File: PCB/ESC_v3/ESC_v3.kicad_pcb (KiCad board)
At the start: 4 copper layers, 42 x 83.5 mm, 133 parts, among them J1 Conn_01x04_Pin, J10 Conn_01x01_Pin, J11 Screw_Terminal_01x01, J2 Screw_Terminal_01x01, J3 Conn_01x01_Pin, J4 Conn_01x01_Pin, J5 Conn_01x01_Pin, J6 Conn_01x01_Pin, J7 Conn_01x01_Pin, J8 Conn_01x01_Pin, J9 Conn_01x01_Pin, Q1 NTMFS2D1N08XT1G, Q2 NTMFS2D1N08XT1G, Q3 NTMFS2D1N08XT1G, Q4 NTMFS2D1N08XT1G, Q5 NTMFS2D1N08XT1G, Q6 NTMFS2D1N08XT1G, U1 SN65HVD232, U2 DRV8323SRTAT, U5 STM32G431CBT6, Y2 16MHz

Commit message: Updates
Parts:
- added C33: 100n, Capacitor_SMD:C_0805_2012Metric, B.Cu at (140.5, 83.0)
- added C34: 100n/6.3V, Capacitor_SMD:C_0805_2012Metric, B.Cu at (138.5, 72.9)
- added C39: 1u/DNP, Capacitor_SMD:C_0805_2012Metric, F.Cu at (149.8, 91.5)
- added C42: 1u/DNP, Capacitor_SMD:C_0805_2012Metric, F.Cu at (149.8, 93.5)
- added C43: 100n, Capacitor_SMD:C_0805_2012Metric, F.Cu at (137.3, 98.3)
- C24, C36, C37: value 0.1uF -> 100n
- C35: value 0.1uF -> 10n
- C38: value 0.1uF -> 4u7
- C40, C41: value 10pF -> 6p8
- Y2: value 16MHz -> 24MHz
- moved C21 2.59 mm to (144.6, 70.2), turned to 90 degrees
- moved C46 2.12 mm to (149.7, 88.2)
- moved C47 1.91 mm to (151.8, 88.8)
- moved L2 1.87 mm to (147.0, 92.2), turned to -90 degrees
- moved C35 1.58 mm to (144.9, 91.6), turned to 90 degrees
- moved C32 1.50 mm to (141.5, 97.5), turned to -90 degrees
- moved R52 1.43 mm to (144.7, 97.3), turned to 90 degrees
- moved R36 1.03 mm to (138.1, 84.1)
- moved R53 0.87 mm to (143.2, 95.6)
- moved R54 0.87 mm to (139.8, 95.7)
- moved C17 0.70 mm to (146.3, 96.8), turned to -90 degrees
- moved R34 0.61 mm to (137.4, 94.2)
- moved R39 0.60 mm to (137.4, 92.7)
- moved R37 0.55 mm to (137.4, 90.8)
- moved R32 0.27 mm to (140.7, 91.7)
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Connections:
- C35 pad 2: 3V3 -> /MCU/VDDA
- L2 pad 1: 3V3 -> /MCU/VDDA
- L2 pad 2: /MCU/VDDA -> 3V3
- U5 pad 20: unconnected-(U5-VREF+-Pad20) -> /MCU/VDDA
- U5 pad 27: unconnected-(U5-PB13-Pad27) -> CAL_DV
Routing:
- net CAL_DV: track 5.47 -> 31.7 mm, vias 1 -> 2
- net 3V3: track 102.7 -> 127.5 mm, vias 7 -> 8
- net nSCS: track 28.0 -> 44.3 mm, vias 0 -> 2
- net GND: track 61.1 -> 67.4 mm, vias 112 -> 127
- net /MCU/NRST: track 38.3 -> 43.0 mm
- net CAN_TX: track 6.94 -> 11.5 mm
- net /MCU/ADC1_IN14: track 45.2 -> 41.3 mm
- net /MCU/VDDA: track 2.39 -> 6.23 mm
- net /MCU/ADC1_IN11: track 44.7 -> 41.1 mm
- net CAN_RX: track 5.58 -> 9.18 mm
- net EN_DV: track 25.4 -> 28.4 mm
- net /MCU/SWCLK: track 35.6 -> 37.6 mm
- net /MCU/USART2_TX: track 35.3 -> 36.5 mm
- net /MCU/USART2_RX: track 28.4 -> 29.2 mm
- net SDI: track 44.8 -> 44.2 mm
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
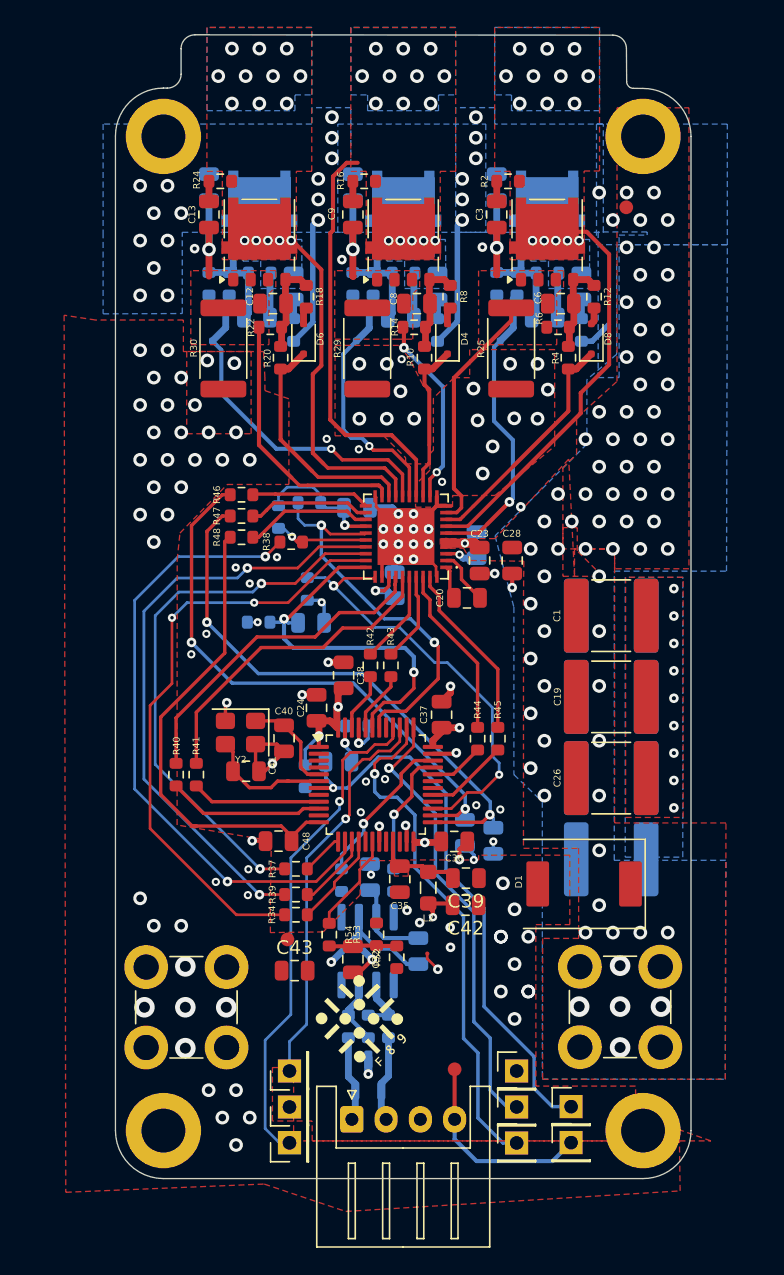
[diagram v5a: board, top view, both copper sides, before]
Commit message: Update PCB layout and driver schematic
Adjust KiCad project files: many PCB footprint positions/rotations/uuids and silk/pad orientations updated, trace segments and widths adjusted, vias added/moved (several tented/free vias), and zone_connect enabled on referenced footprints. Correct MCU pin net assignments (PB4/PB5/PB6 / NFAULT / EN_DV) and other net fixes. In DRVR schematic change stroke styles to dashed and update a capacitor value from ">=10uF" to "22u". Remove several old backup zip files and add new backup snapshots. Miscellaneous small .kicad_prl/.kicad_sch/.ioc updates included for consistency and routing cleanup.
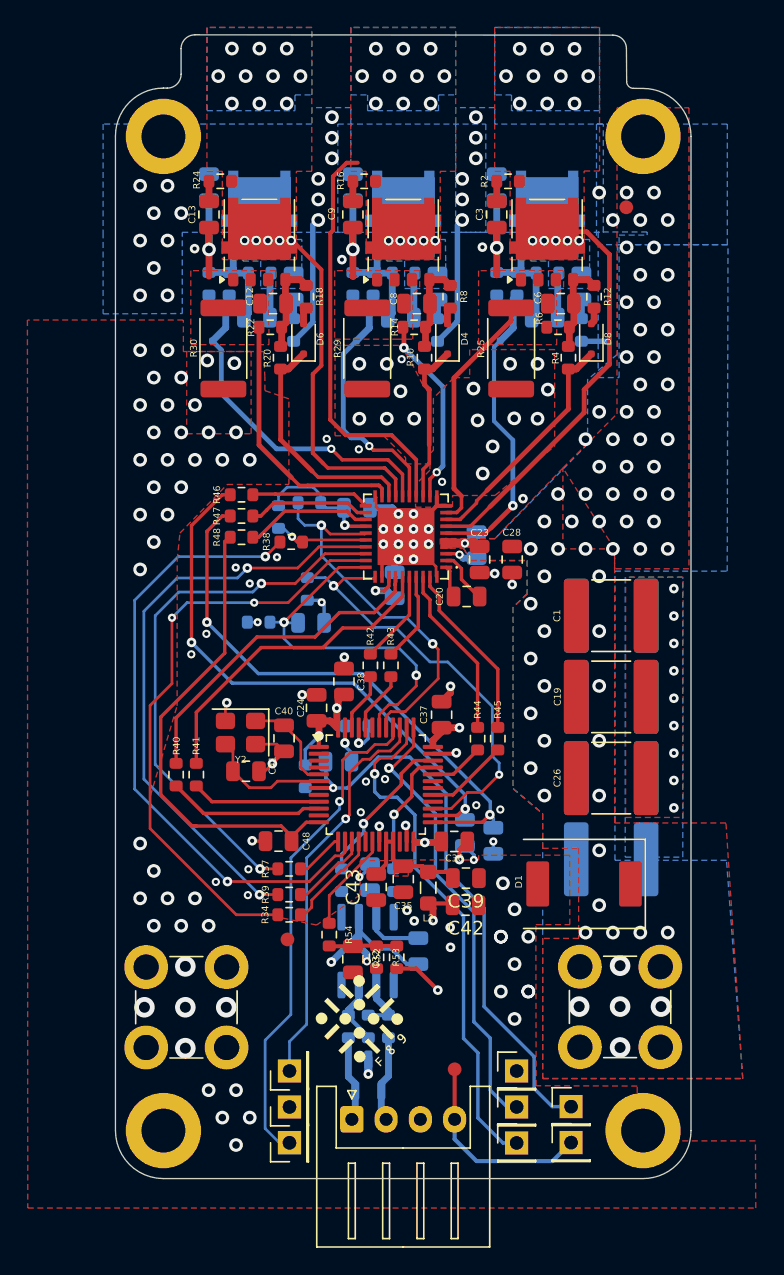
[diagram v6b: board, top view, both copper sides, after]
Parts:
- moved C43 8.52 mm to (143.2, 92.2), turned to 90 degrees
- moved R53 1.67 mm to (143.2, 97.3), turned to -90 degrees
- moved R34 0.50 mm to (136.9, 94.2)
- moved R37 0.50 mm to (136.9, 90.8)
- moved R39 0.50 mm to (136.9, 92.7)
- moved C38 0.45 mm to (140.9, 77.2)
- moved C35 0.25 mm to (145.2, 91.6)
- moved C20 0.10 mm to (149.8, 71.0)
- moved C23 0.07 mm to (150.8, 68.3)
- moved C28 0.07 mm to (153.2, 68.3)
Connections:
- U5 pad 41: unconnected-(U5-PB4-Pad41) -> NFAULT
- U5 pad 42: NFAULT -> EN_DV
- U5 pad 43: EN_DV -> unconnected-(U5-PB6-Pad43)
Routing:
- net GND: track 67.4 -> 64.0 mm, vias 127 -> 133
- net /MCU/VDDA: track 6.23 -> 9.39 mm
- net EN_DV: track 28.4 -> 27.4 mm
- net 3V3: track 127.5 -> 128.5 mm
- net NFAULT: track 28.7 -> 28.1 mm
- net nSCS: track 44.3 -> 43.8 mm
- net SDI: track 44.2 -> 43.7 mm
- net SCLK: track 40.7 -> 40.2 mm
- net /MCU/SPI1_SCK: track 3.07 -> 3.57 mm

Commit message: Reposition DRVR schematic elements
Adjust layout in PCB/ESC_v3/DRVR.kicad_sch: updated coordinates for rectangles, text labels, junctions, wires and pins to tidy and realign the driver schematic. Changes are graphical/coordinate-only (no netlist/electrical changes). Also touched project files (ESC_v3.*) and refreshed backup archives (deleted several older backups and added new snapshots).
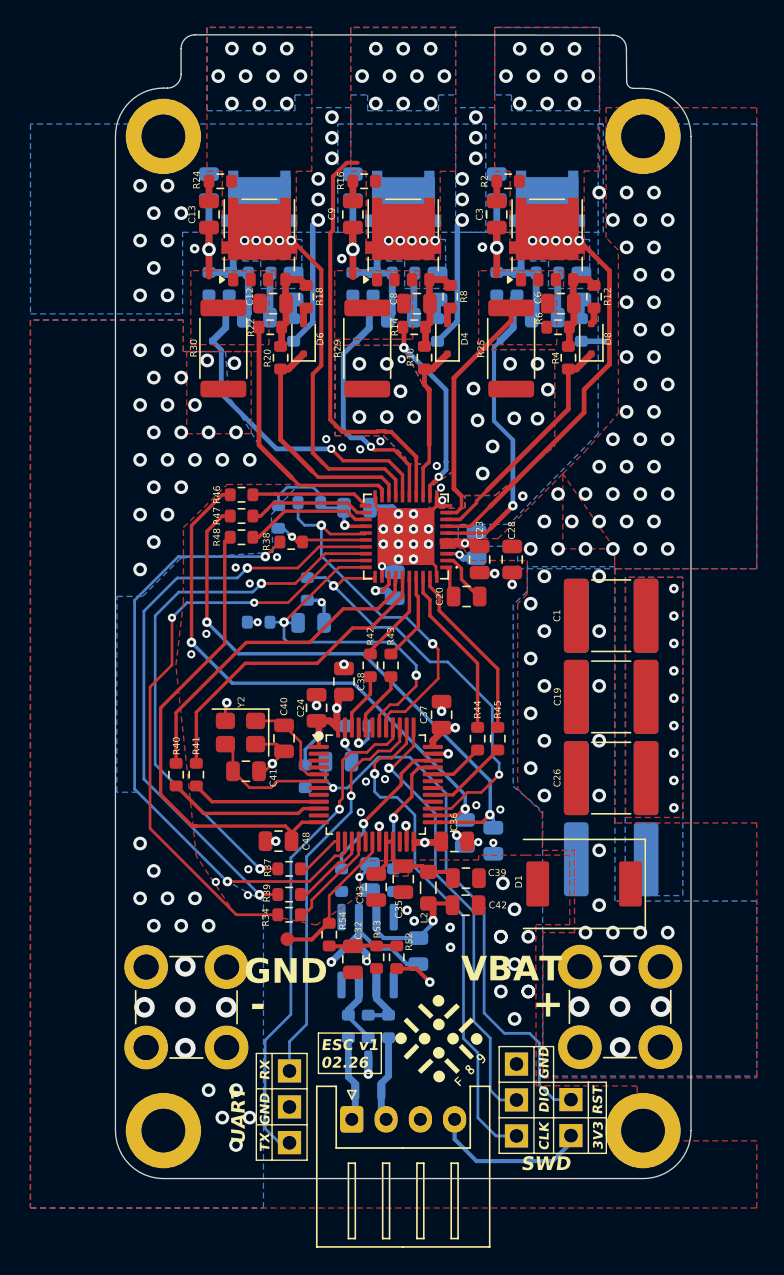
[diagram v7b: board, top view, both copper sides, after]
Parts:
- removed the ? at (148.9, 105.5)
- removed REF**: TestPoint_Pad_D1.0mm, TestPoint:TestPoint_Pad_D1.0mm
- added G***: LOGO, LOGO, B.Cu at (130.2, 82.2)
- moved G*** 5.97 mm to (147.9, 103.3)
- moved J4 0.51 mm to (157.4, 110.3)
- moved J7 0.51 mm to (157.4, 107.7)
- moved J3 0.51 mm to (153.5, 105.1)
- moved J5 0.51 mm to (153.5, 110.3)
- moved J6 0.51 mm to (153.5, 107.7)
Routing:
- net GND: track 64.0 -> 56.8 mm, vias 133 -> 138
- net SPC: track 31.8 -> 26.6 mm
- net V_BAT_MEAS: track 7.27 -> 10.8 mm
- net 3V3: track 128.5 -> 126.3 mm
- net /MCU/ADC1_IN14: track 41.3 -> 42.2 mm
- net V_A_PHASE: track 34.3 -> 33.6 mm
- net V_BAT: vias 92 -> 90
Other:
- board text added: "+"
- board text added: "-"
- board text added: "3V3"
- board text added: "CLK"
- board text added: "DIO"
- board text added: "ESC v1 02.26"
- board text added: "GND"
- board text added: "RST"
- board text added: "RX"
- board text added: "SWD"
- board text added: "TX"
- board text added: "UART"
- board text added: "VBAT"

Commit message: Update ESC_v3 schematics and PCB layout
Add net-tie symbol and +3V3/GND1 power symbols to DRVR schematic and reorganize schematic graphics (rectangles, text), junctions, and wires with updated coordinates/UUIDs. Also update top-level ESC_v3 schematic and MCU schematic along with PCB (.kicad_pcb) and panel (.kicad_prl) files. Remove several old backup zip files and add new backups for the ESC_v3 project.
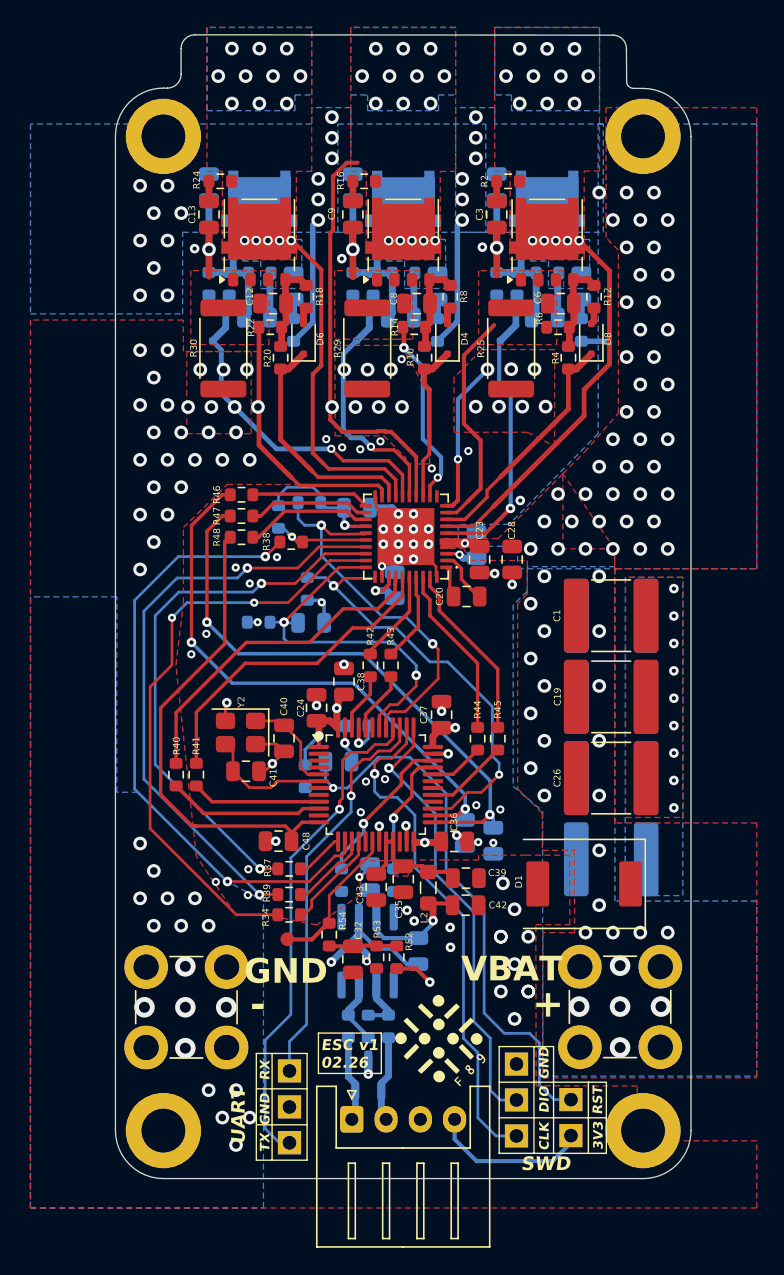
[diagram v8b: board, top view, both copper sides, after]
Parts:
- C28: value >=10uF -> 22u
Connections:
- net /MCU/ADC1_IN11 renamed ADC1_IN11
- net /MCU/ADC1_IN14 renamed ADC1_IN14
- net /MCU/ADC2_IN12 renamed ADC2_IN12
- net /MCU/BOOT0 renamed BOOT0
- net /MCU/NRST renamed NRST
- net /MCU/OSC_IN renamed OSC_IN
- net /MCU/OSC_OUT renamed OSC_OUT
- net /MCU/SPI1_MISO renamed SPI1_MISO
- net /MCU/SPI1_MOSI renamed SPI1_MOSI
- net /MCU/SPI1_NSS/CS renamed SPI1_NSS/CS
- net /MCU/SPI1_SCK renamed SPI1_SCK
- net /MCU/SWCLK renamed SWCLK
- net /MCU/SWDIO renamed SWDIO
- net /MCU/TIM15_CH1 renamed TIM15_CH1
- net /MCU/TIM15_CH1N renamed TIM15_CH1N
- net /MCU/TIM17_CH1 renamed TIM17_CH1
- net /MCU/TIM17_CH1N renamed TIM17_CH1N
- net /MCU/TIM1_CH3 renamed TIM1_CH3
- net /MCU/TIM1_CH3N renamed TIM1_CH3N
- net /MCU/USART2_RX renamed USART2_RX
- net /MCU/USART2_TX renamed USART2_TX
- net /MCU/VDDA renamed VDDA
- net 3V3 renamed VDD
- net CAL_DV renamed CAL
- net EN_DV renamed ENABLE
- R25 pad 2: GND -> SNA
- R29 pad 2: GND -> SNB
- R30 pad 2: GND -> SNC
- U2 pad 10: GND -> SNA
- U2 pad 11: GND -> SNB
- U2 pad 20: GND -> SNC
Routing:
- net SNA: track 0.00 -> 11.5 mm, vias 0 -> 1
- net GND: track 56.8 -> 54.2 mm, vias 138 -> 139
